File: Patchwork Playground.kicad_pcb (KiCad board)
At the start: 2 copper layers, 100 x 60 mm, 90 parts, among them J1 PADS, J2 USB_C_Receptacle_USB2.0, J3 PADS, J4 POGO, J5 PADS, J6 JST-GH-4P, SW1 SW_SPDT, SW2 SW_SPDT, SW3 SW_SPDT, SW4 BUTTON, SW5 SW_SPDT, SW6 SW_SPDT, SW7 SW_SPDT, U1 SMF05CT1G, U2 M3406, U3 BQ21040DBVR, U4 SMF05CT1G, U5 QMC5883L, U6 BC805M, U7 LSM6DSV

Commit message: prettify
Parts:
- removed the R23 at (117.6, 120.4)
- removed the R4 at (189.4, 83.9)
- removed the R9 at (189.4, 81.9)
- added R10: 200k, Patchwork Playground Footprints:R_0603_1608Metric, F.Cu at (183.6, 79.1)
- added R11: 200k, Patchwork Playground Footprints:R_0603_1608Metric, F.Cu at (181.6, 79.1)
- added R26: 200k, Patchwork Playground Footprints:R_0603_1608Metric, F.Cu at (114.8, 121.2)
- added R27: 200k, Patchwork Playground Footprints:R_0603_1608Metric, F.Cu at (117.6, 120.4)
- added R3: 200k, Patchwork Playground Footprints:R_0603_1608Metric, F.Cu at (186.4, 83.9)
- added R30: 200k, Patchwork Playground Footprints:R_0603_1608Metric, F.Cu at (123.8, 119.7)
- added R5: 200k, Patchwork Playground Footprints:R_0603_1608Metric, F.Cu at (186.4, 81.9)
- moved TP4 3.33 mm to (182.6, 82.7)
- renumbered C5 to C4, C4 to C5, R10 to R12, R11 to R13, R12 to R14, R13 to R15, R14 to R16, R15 to R17, R16 to R18, R17 to R19, R18 to R20, R19 to R21, R20 to R22, R21 to R23, R22 to R24, R24 to R25, R25 to R28, R26 to R29, R27 to R31, R28 to R32, R3 to R4, R5 to R6, R6 to R7, R7 to R8, R8 to R9
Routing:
- net Net-(U2-FB): track 6.01 -> 11.0 mm
- net Net-(R3-Pad1): track 0.00 -> 3.44 mm
- net +BATT: track 138.0 -> 134.6 mm
- net Net-(R26-Pad2): track 0.00 -> 2.01 mm
- net ADC: track 41.7 -> 40.9 mm
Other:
- board text added: "+"
- board text added: "0x68"
- board text added: "0x69"
- board text added: "3V3"
- board text added: "5V"
- board text added: "5V POWER INPUTS"
- board text added: "ADC"
- board text added: "BAT"
- board text added: "BATTERY"
- board text added: "BUCK"
- board text added: "CHARGER"
- board text added: "CLK"
- board text added: "COM"
- board text added: "CURRENT"
- board text added: "Development board - not for consumer use"
- board text added: "ESD"
- board text added: "GLOBAL POWER"
- board text added: "I2C"
- board text added: "IMU Address"
- board text added: "INT"
- board text added: "IO"
- board text added: "KOUNO"
- board text added: "LAB"
- board text added: "LSM6DSV"
- board text added: "MAIN I2C"
- board text added: "POGO"
- board text added: "Patchwork Playground"
- board text added: "QMC5883L"
- board text added: "SCL"
- board text added: "SCX"
- board text added: "SDA"
- board text added: "SDX"
- board text added: "SENSORHUB"
- board text added: "SWD"
- board text added: "USB-C"
- board text added: "USER IO"
- board text added: "v1.0"
- board text removed: "locked"

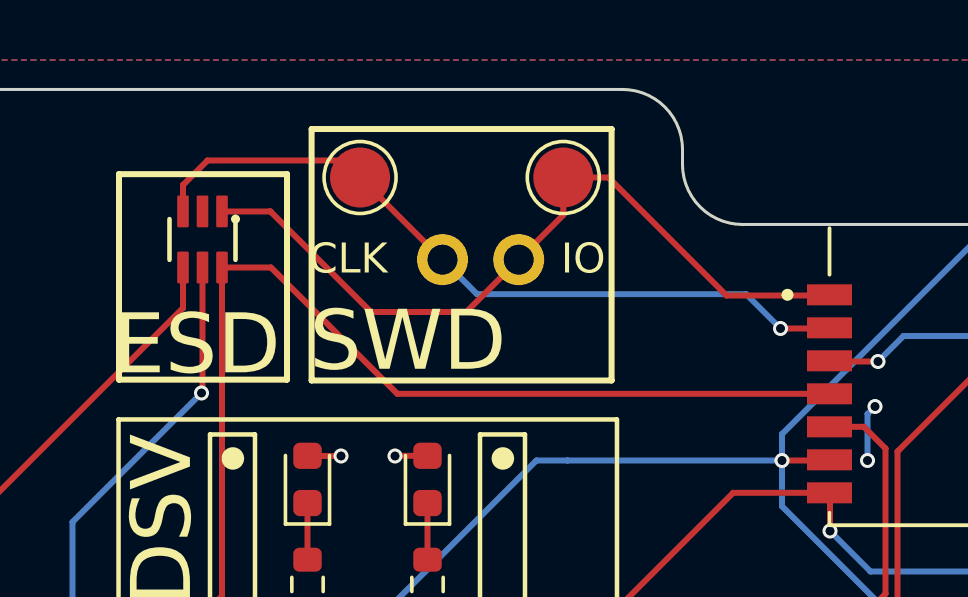
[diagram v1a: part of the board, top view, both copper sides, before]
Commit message: change swd footprint
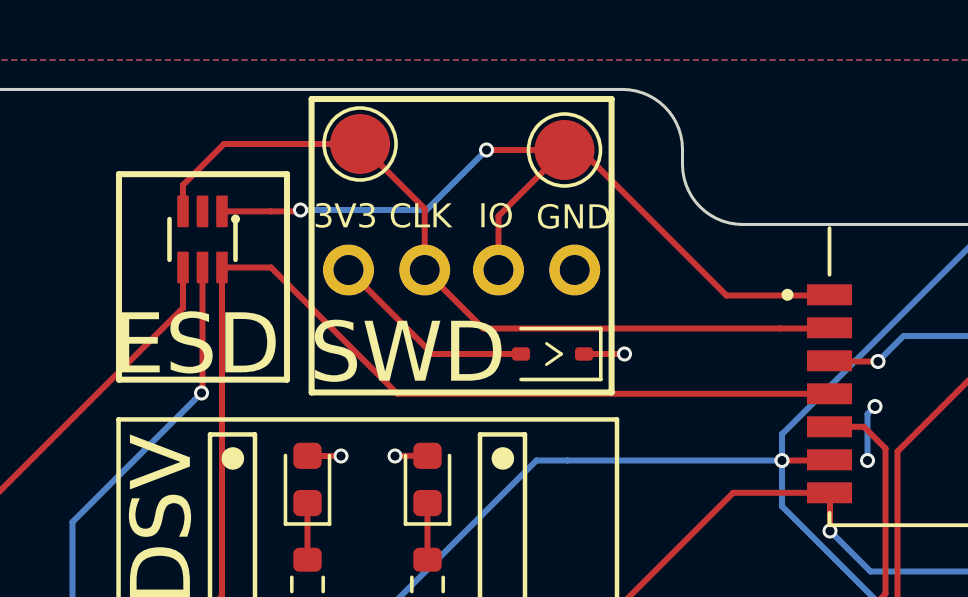
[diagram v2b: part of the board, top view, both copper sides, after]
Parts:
- added D1: B5817WS, Patchwork Playground Footprints:D_SOD-323, F.Cu at (133.6, 79.8)
- added J2: PADS, Patchwork Playground Footprints:PinHeader_1x02_P2.54mm_Vertical, F.Cu at (131.8, 77.0)
- moved J1 3.15 mm to (126.8, 77.0)
- moved TP12 1.12 mm to (127.2, 72.8)
- moved TP11 0.92 mm to (134.0, 73.0)
- renumbered D9 to D10, D10 to D11, D11 to D12, D12 to D13, D13 to D14, D1 to D2, D2 to D3, D3 to D4, D4 to D5, D5 to D6, D6 to D7, D7 to D8, D8 to D9, J2 to J3, J3 to J4, J4 to J5, J5 to J6, J6 to J7
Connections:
- J1 pad 1: SWCLK -> Net-(D1-A)
- J1 pad 2: SWDIO -> SWCLK
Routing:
- net Net-(D1-A): track 0.00 -> 6.91 mm
- net SWDIO: track 25.9 -> 28.0 mm, vias 0 -> 2
- net SWCLK: track 25.1 -> 26.8 mm, vias 1 -> 0
- net VDD: track 50.1 -> 51.5 mm, vias 22 -> 23
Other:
- board text added: "GND"

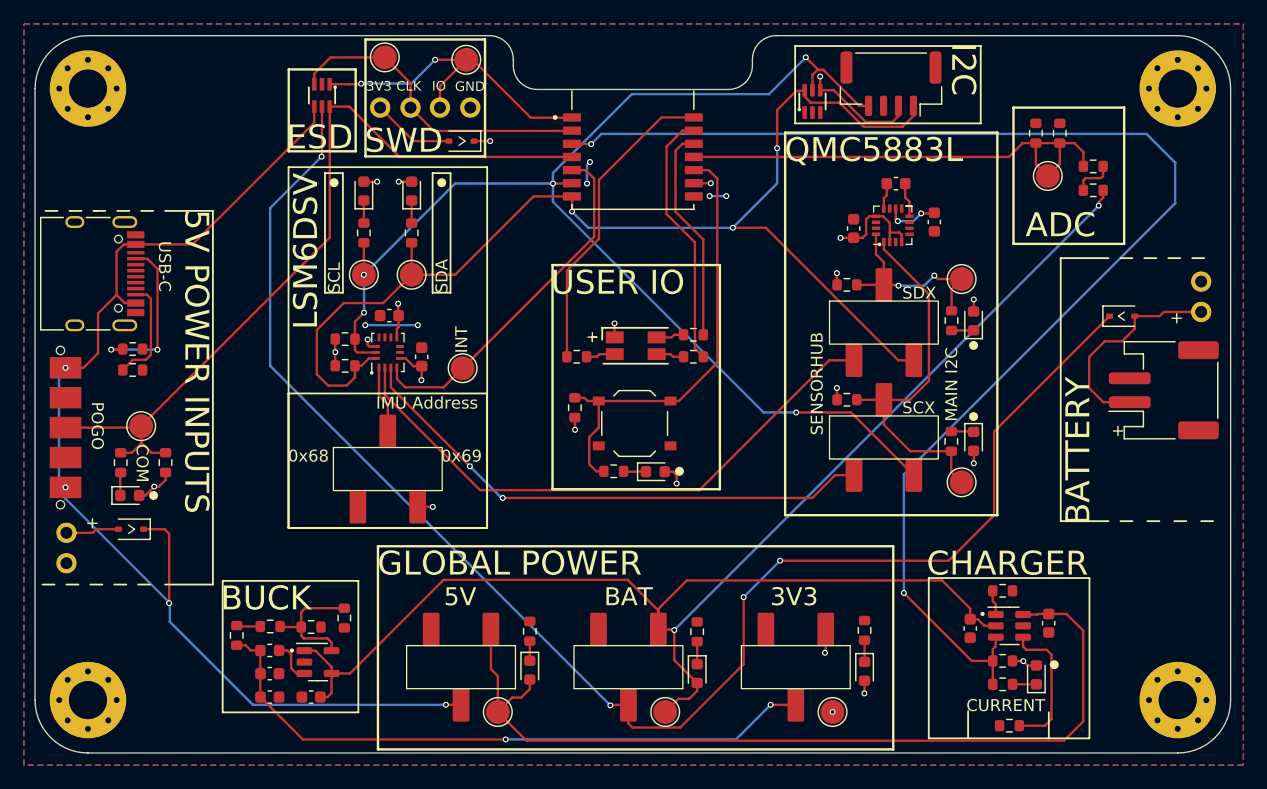
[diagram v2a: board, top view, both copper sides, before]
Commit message: change adc/buck res values, fix qmc sensorhub pullups
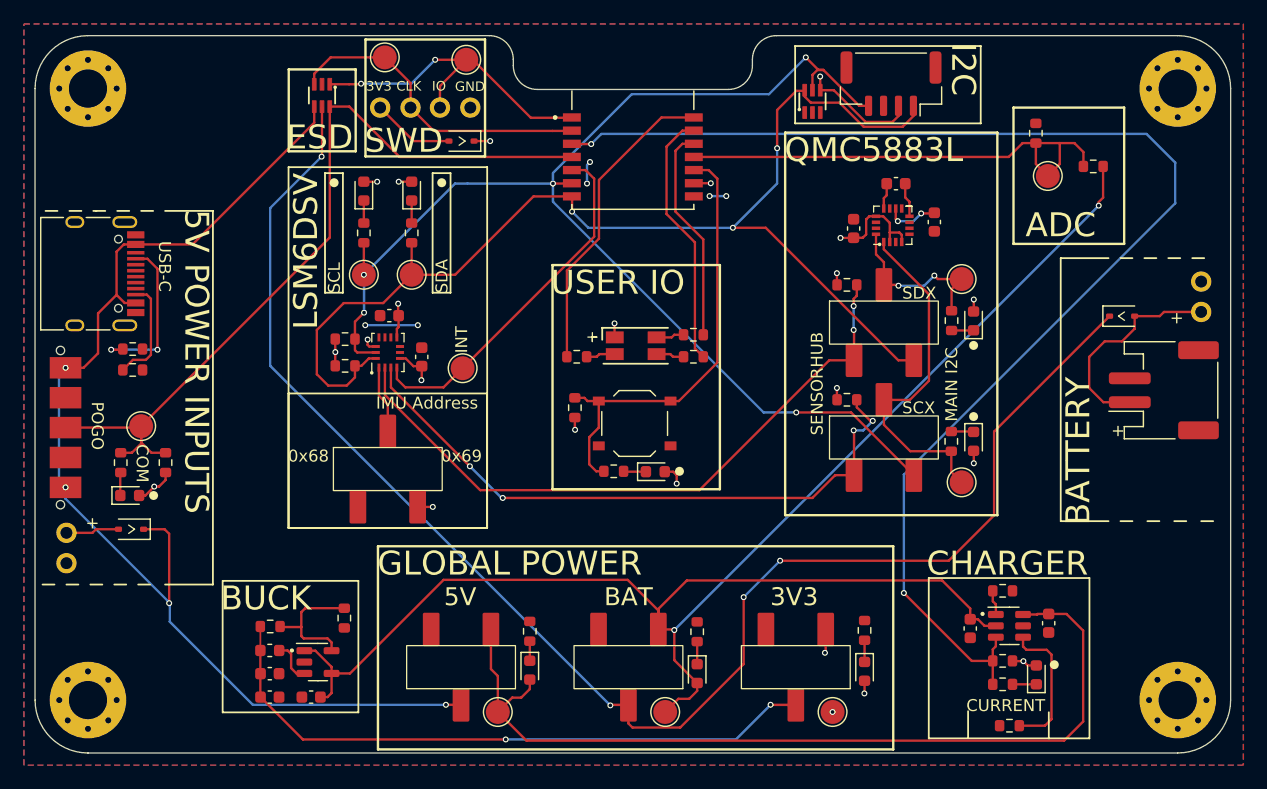
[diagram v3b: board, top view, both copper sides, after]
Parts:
- removed the R10 at (183.6, 79.1)
- removed the R25 at (121.0, 120.4)
- removed the R26 at (114.8, 121.2)
- removed the R3 at (186.4, 83.9)
- R22: renamed from R27; value 200k -> 1M
- R23: renamed from R30; value 200k -> 330k
- R4: renamed from R5; value 200k -> 470k
- R9: renamed from R11; value 200k -> 330k
- renumbered C5 to C4, C4 to C5, R12 to R10, R13 to R11, R15 to R12, R16 to R13, R18 to R15, R17 to R16, R20 to R17, R19 to R18, R22 to R19, R21 to R20, R24 to R21, R23 to R24, R29 to R25, R28 to R26, R32 to R27, R31 to R28, R4 to R3, R6 to R5, R7 to R6, R8 to R7, R9 to R8
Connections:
- R18 pad 1: SDX -> SENSORHUB_SDA
- R20 pad 1: SCX -> SENSORHUB_SCL
- R22 pad 1: Net-(R26-Pad2) -> +3V3
- R4 pad 2: Net-(R3-Pad1) -> +BATT
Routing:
- net SENSORHUB_SCL: track 45.0 -> 53.1 mm, vias 2 -> 4
- net SENSORHUB_SDA: track 49.3 -> 55.8 mm, vias 0 -> 2
- net Net-(R3-Pad1): track 3.44 -> 0.00 mm
- net SDX: track 16.8 -> 14.5 mm
- net SCX: track 31.5 -> 29.2 mm
- net Net-(R26-Pad2): track 2.01 -> 0.00 mm
- net +BATT: track 134.6 -> 136.6 mm

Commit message: fix fix fix fix fix
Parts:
- L1: value 2u2H -> 4u7H
- R22: value 1M -> 2M
- R23: value 330k -> 470k
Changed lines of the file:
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@@
     (tags "inductor")
     (property "EXTENDED?" "YES")
-    (property "MPN" "C285966")
+    (property "MPN" "C1034")
     (property "Sheetfile" "Patchwork Playground.kicad_sch")
     (property "Sheetname" "")
@@
         (effects (font (size 1 1) (thickness 0.15)))
     )
-    (fp_text value "2u2H" (at 0 1.43) (layer "F.Fab") hide
+    (fp_text value "4u7H" (at 0 1.43) (layer "F.Fab") hide
         (effects (font (size 1 1) (thickness 0.15)))
     )
@@
     (tags "resistor")
     (property "EXTENDED?" "")
-    (property "MPN" "C22935")
+    (property "MPN" "C22976")
     (property "Sheetfile" "Patchwork Playground.kicad_sch")
     (property "Sheetname" "")
@@
         (effects (font (size 1 1) (thickness 0.15)))
     )
-    (fp_text value "1M" (at 0 1.43 180) (layer "F.Fab") hide
+    (fp_text value "2M" (at 0 1.43 180) (layer "F.Fab") hide
         (effects (font (size 1 1) (thickness 0.15)))
     )
@@
     (tags "resistor")
     (property "EXTENDED?" "")
-    (property "MPN" "C23137")
+    (property "MPN" "C23178")
     (property "Sheetfile" "Patchwork Playground.kicad_sch")
     (property "Sheetname" "")
@@
         (effects (font (size 1 1) (thickness 0.15)))
     )
-    (fp_text value "330k" (at 0 1.43 90) (layer "F.Fab") hide
+    (fp_text value "470k" (at 0 1.43 90) (layer "F.Fab") hide
         (effects (font (size 1 1) (thickness 0.15)))
     )

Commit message: v1.1
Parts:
- removed the D5 at (188.9, 94.4)
- removed the D7 at (148.2, 96.9)
- removed the J2 at (131.8, 77.0)
- removed the R14 at (123.9, 98.6)
- removed the R16 at (123.9, 96.4)
- removed R24, R26, R28: 10k, Patchwork Playground Footprints:R_0603_1608Metric
- added C1: 100nF, Patchwork Playground Footprints:C_0603_1608Metric, F.Cu at (169.0, 77.2)
- added D6: RGB, Patchwork Playground Footprints:LED_RGB_1210, F.Cu at (155.7, 96.3)
- added SW4: BUTTON, Patchwork Playground Footprints:SW_Push_1P1T_XKB_TS-1187A, F.Cu at (102.3, 117.1)
- C2: renamed from C1; value 4u7F -> 4.7uF
- C3: renamed from C2; value 4u7F -> 4.7uF
- C4: renamed from C3; value 4u7F -> 4.7uF
- C5: renamed from C4; value 4u7F -> 4.7uF
- C6: renamed from C5; value 4u7F -> 4.7uF
- C8: renamed from C7; value 4u7F -> 4.7uF
- C9: renamed from C8; value 0u22F -> 220nF
- J1: value PADS -> SWD_HEADER; footprint Patchwork Playground Footprints:PinHeader_1x02_P2.54mm_Vertical -> Patchwork Playground Footprints:PinHeader_1x04_P2.54mm_Vertical
- L1: value 4u7H -> 4.7uH
- moved J6 29.3 mm to (194.5, 90.3), turned to 90 degrees
- moved U4 28.3 mm to (190.1, 84.6), turned to -90 degrees
- moved D7 21.3 mm to (142.3, 101.0), turned to 0 degrees
- moved D8 21.3 mm to (142.3, 97.0), turned to 0 degrees
- moved R12 16.4 mm to (138.8, 101.0), turned to 0 degrees
- moved R14 16.4 mm to (138.8, 97.0), turned to 0 degrees
- moved R4 14.8 mm to (172.4, 77.2), turned to -90 degrees
- moved TP4 14.7 mm to (170.8, 74.0), turned to -90 degrees
- moved BT1 13.3 mm to (192.6, 113.9)
- moved J5 12.9 mm to (195.9, 106.9)
- moved D12 12.2 mm to (109.5, 97.8), turned to -90 degrees
- moved TP6 11.6 mm to (135.3, 101.0), turned to -90 degrees
- moved TP7 11.6 mm to (135.3, 97.0), turned to -90 degrees
- moved R9 11.1 mm to (170.8, 77.2), turned to 90 degrees
- moved SW6 10.7 mm to (120.6, 99.0), turned to -90 degrees
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- renumbered C9 to C10, C10 to C11, C6 to C7, D11 to D10, D12 to D11, D13 to D12, D14 to D13, D6 to D5, D8 to D7, D9 to D8, D10 to D9, J3 to J2, J4 to J3, J5 to J4, J6 to J5, J7 to J6, R15 to R14, R17 to R15, R19 to R16, R22 to R17, R23 to R18, R21 to R19, R25 to R20, R27 to R21, R18 to R22, R20 to R23, SW4 to SW5, SW5 to SW6, SW6 to SW7, SW7 to SW8
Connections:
- net CHRG_STATUS renamed CHRG
- net COM renamed DOCK
- BT1 pad 1: Net-(BT1-+) -> VDC
- J5 pad 1: Net-(BT1-+) -> VDC
- R21 pad 1: BUTTON -> BTN
- SW5 pad 2: BUTTON -> BTN
- TP5 pad 1: LSM_INT -> INT
- U6 pad 10: BUTTON -> ADC
- U6 pad 11: ADC -> LED_BLUE
- U6 pad 12: LED_BLUE -> LED_GREEN
- U6 pad 13: LED_GREEN -> LED_RED
- U6 pad 14: LED_RED -> BTN
- U6 pad 5: LSM_INT -> SCL
- U6 pad 6: SCL -> SDA
- U6 pad 7: SDA -> INT
- U7 pad 4: LSM_INT -> INT
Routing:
- net CHRG: track 111.1 -> 61.2 mm
- net BTN: track 0.00 -> 46.6 mm
- net BUTTON: track 38.1 -> 0.00 mm
- net INT: track 0.00 -> 37.7 mm, vias 0 -> 2
- net LSM_INT: track 30.0 -> 0.00 mm
- net Net-(BT1-+): track 18.0 -> 0.00 mm
- net DOCK: track 68.9 -> 84.6 mm, vias 0 -> 2
- net +BATT: track 136.6 -> 123.4 mm, vias 2 -> 6
- net ADC: track 40.9 -> 28.9 mm, vias 0 -> 3
- net VCC: track 75.3 -> 63.5 mm, vias 0 -> 2
- net SDA: track 100.4 -> 111.1 mm, vias 3 -> 6
- net SENSORHUB_SDA: track 55.8 -> 65.5 mm, vias 2 -> 0
- net Net-(U2-FB): track 11.0 -> 3.44 mm
- net LED_RED: track 26.0 -> 18.9 mm
- net SENSORHUB_SCL: track 53.1 -> 59.9 mm, vias 4 -> 2
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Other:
- board text added: "locked"
- board text added: "v1.1"
- board text removed: "+"
- board text removed: "0x68"
- board text removed: "0x69"
- board text removed: "3V3"
- board text removed: "5V"
- board text removed: "5V POWER INPUTS"
- board text removed: "ADC"
- board text removed: "BAT"
- board text removed: "BATTERY"
- board text removed: "BUCK"
- board text removed: "CHARGER"
- board text removed: "CLK"
- board text removed: "COM"
- board text removed: "CURRENT"
- board text removed: "ESD"
- board text removed: "GLOBAL POWER"
- board text removed: "GND"
- board text removed: "I2C"
- board text removed: "IMU Address"
- board text removed: "INT"
- board text removed: "IO"
- board text removed: "LSM6DSV"
- board text removed: "MAIN I2C"
- board text removed: "POGO"
- board text removed: "QMC5883L"
- board text removed: "SCL"
- board text removed: "SCX"
- board text removed: "SDA"
- board text removed: "SDX"
- board text removed: "SENSORHUB"
- board text removed: "SWD"
- board text removed: "USB-C"
- board text removed: "USER IO"
- board text removed: "v1.0"
